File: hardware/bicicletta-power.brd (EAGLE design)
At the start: 160 x 100 mm, 24 parts, among them IC1 LM5017, IC2 LM1117-3.3

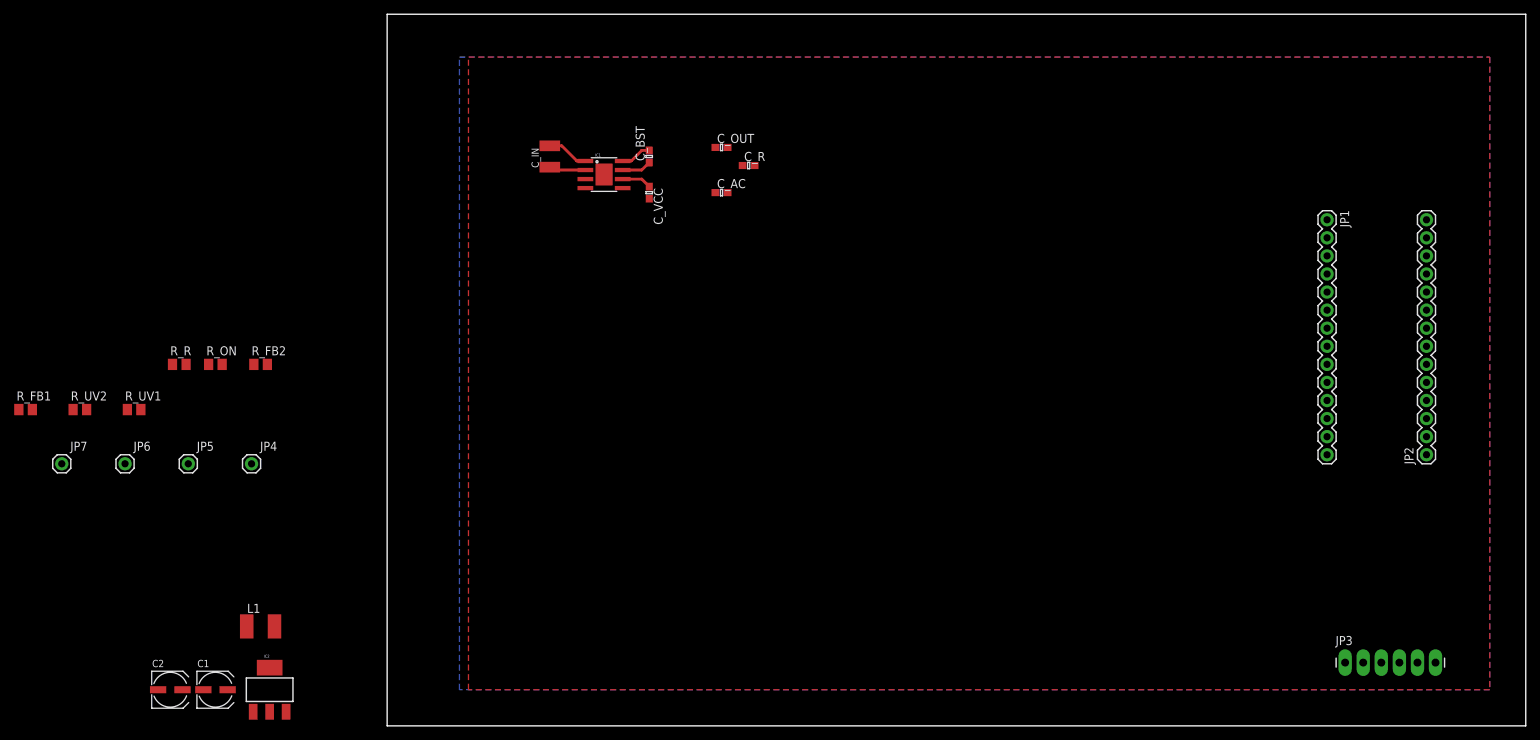
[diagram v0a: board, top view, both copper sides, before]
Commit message: Close to final layout on switching regulator.
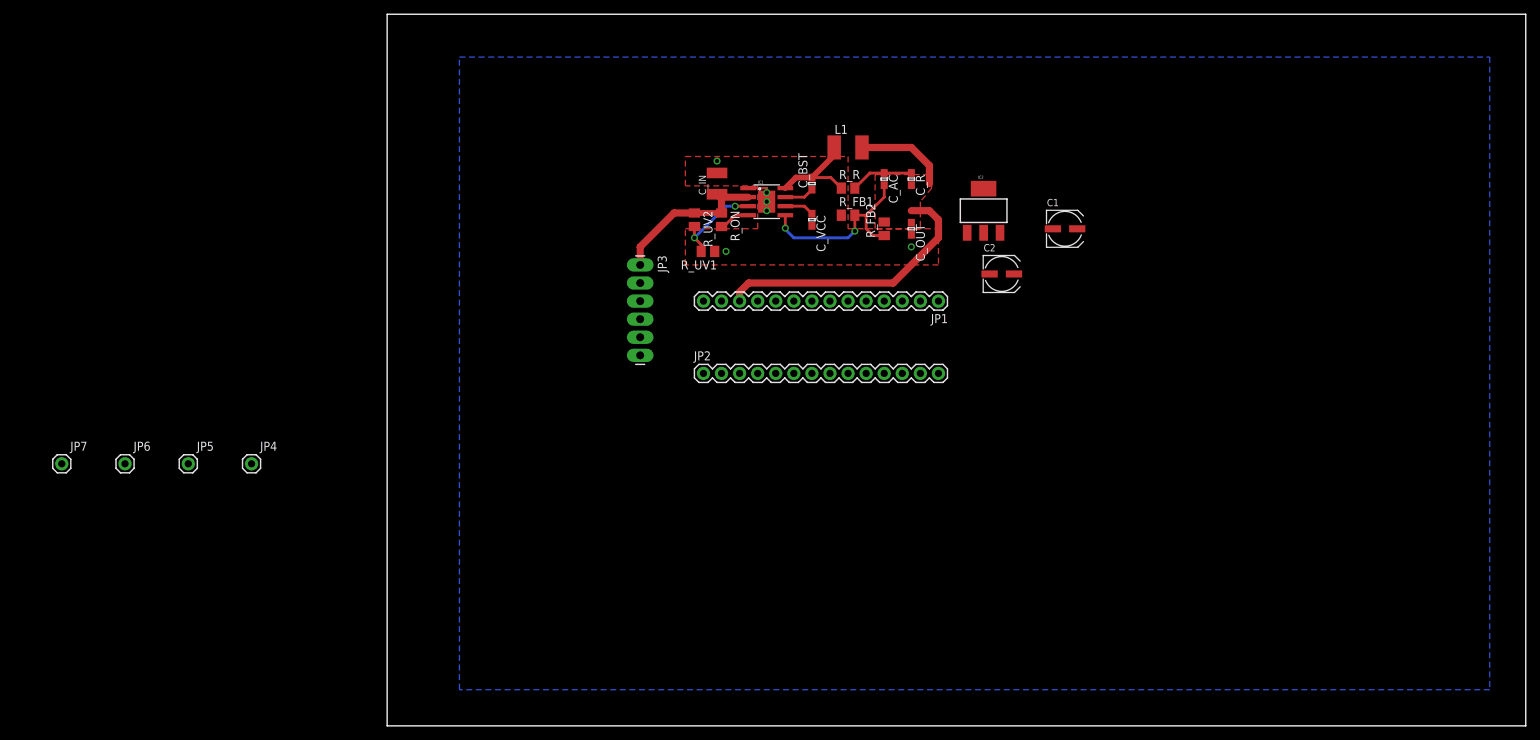
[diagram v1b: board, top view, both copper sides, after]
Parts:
- moved C1 135.8 mm to (95.2, 69.8)
- moved C2 130.6 mm to (86.4, 63.5)
- moved IC2 120.8 mm to (83.8, 72.4)
- moved R_FB1 118.8 mm to (64.8, 71.8)
- moved JP3 113.7 mm to (35.6, 64.8), turned to 270 degrees
- moved L1 106.5 mm to (64.8, 81.3)
- moved JP2 102.2 mm to (44.5, 49.5), turned to 0 degrees
- moved R_R 97.2 mm to (64.8, 75.6)
- moved R_UV2 90.4 mm to (43.2, 71.1), turned to 270 degrees
- moved R_FB2 89.7 mm to (69.8, 69.8), turned to 90 degrees
- moved R_UV1 83.7 mm to (45.1, 66.7), turned to 180 degrees
- moved R_ON 74.0 mm to (47.0, 71.1), turned to 270 degrees
- moved JP1 55.8 mm to (77.5, 59.7), turned to 180 degrees
- moved C_OUT 29.0 mm to (73.7, 69.8), turned to 270 degrees
- moved C_IN 23.8 mm to (46.4, 76.2)
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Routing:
- net 5V: track 0.00 -> 52.3 mm
- net N$2: track 0.00 -> 26.6 mm, vias 0 -> 2
- net V_BATT: track 5.17 -> 23.4 mm
- net N$3: track 0.00 -> 13.3 mm, vias 0 -> 2
- net N$4: track 4.35 -> 14.6 mm
- net N$6: track 0.00 -> 8.82 mm
- net N$1: track 0.00 -> 4.39 mm
- net GND: track 5.89 -> 3.25 mm, vias 0 -> 6
- added copper zone on layer 1, net GND

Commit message: Fine tuning
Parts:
- moved JP7 89.3 mm to (40.6, 59.7)
- moved JP6 78.3 mm to (38.1, 59.7)
- moved JP5 67.3 mm to (38.1, 49.5)
- moved JP4 61.0 mm to (40.6, 49.5)
- moved JP3 11.5 mm to (36.8, 76.2)
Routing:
- net V_BATT: track 23.4 -> 20.2 mm
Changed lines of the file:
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@@
 <element name="C_R" library="rcl" package="C0603" value="3300pF" x="73.66" y="76.835" rot="R270"/>
 <element name="C_AC" library="rcl" package="C0603" value="100nF" x="69.85" y="76.835" rot="R270"/>
-<element name="JP3" library="SparkFun-Connectors" package="1X06_LONGPADS" value="" x="35.56" y="64.77" rot="R270"/>
-<element name="JP4" library="SparkFun-Connectors" package="1X01" value="M01PTH" x="-19.05" y="36.83"/>
-<element name="JP5" library="SparkFun-Connectors" package="1X01" value="M01PTH" x="-27.94" y="36.83"/>
-<element name="JP6" library="SparkFun-Connectors" package="1X01" value="M01PTH" x="-36.83" y="36.83"/>
-<element name="JP7" library="SparkFun-Connectors" package="1X01" value="M01PTH" x="-45.72" y="36.83"/>
+<element name="JP3" library="SparkFun-Connectors" package="1X06_LONGPADS" value="" x="36.83" y="76.2" rot="R270"/>
+<element name="JP4" library="SparkFun-Connectors" package="1X01" value="M01PTH" x="40.64" y="49.53"/>
+<element name="JP5" library="SparkFun-Connectors" package="1X01" value="M01PTH" x="38.1" y="49.53"/>
+<element name="JP6" library="SparkFun-Connectors" package="1X01" value="M01PTH" x="38.1" y="59.69"/>
+<element name="JP7" library="SparkFun-Connectors" package="1X01" value="M01PTH" x="40.64" y="59.69"/>
 </elements>
 <signals>
@@
 </polygon>
 <polygon width="0.4064" layer="1" thermals="no">
-<vertex x="41.91" y="80.01"/>
+<vertex x="44.45" y="80.01"/>
 <vertex x="64.77" y="80.01"/>
 <vertex x="64.77" y="69.85"/>
@@
 <vertex x="52.07" y="69.85"/>
 <vertex x="52.07" y="75.8825"/>
-<vertex x="41.91" y="75.8825"/>
+<vertex x="44.45" y="75.8825"/>
 </polygon>
 <via x="53.34" y="73.66" extent="1-16" drill="0.6"/>
@@
 <contactref element="JP7" pad="1"/>
 <wire x1="43.18" y1="72.07" x2="46.99" y2="72.07" width="0.8128" layer="1"/>
-<wire x1="35.56" y1="64.77" x2="35.56" y2="67.31" width="1.016" layer="1"/>
-<wire x1="35.56" y1="67.31" x2="40.32" y2="72.07" width="1.016" layer="1"/>
-<wire x1="43.18" y1="72.07" x2="40.32" y2="72.07" width="1.016" layer="1"/>
+<wire x1="36.83" y1="76.2" x2="40.64" y2="76.2" width="1.016" layer="1"/>
+<wire x1="40.64" y1="76.2" x2="43.1775" y2="73.6575" width="1.016" layer="1"/>
+<wire x1="43.18" y1="72.07" x2="43.1775" y2="73.6575" width="1.016" layer="1"/>
 <wire x1="46.99" y1="72.07" x2="46.99" y2="74.065" width="1.016" layer="1"/>
 <wire x1="46.99" y1="74.065" x2="46.355" y2="74.7" width="1.016" layer="1"/>
 <wire x1="50.7238" y1="74.295" x2="46.76" y2="74.295" width="1.016" layer="1"/>
 <wire x1="46.76" y1="74.295" x2="46.355" y2="74.7" width="1.016" layer="1"/>
-<wire x1="-36.83" y1="36.83" x2="35.56" y2="64.77" width="0" layer="19" extent="1-1"/>
-<wire x1="-45.72" y1="36.83" x2="-36.83" y2="36.83" width="0" layer="19" extent="1-1"/>
+<wire x1="40.64" y1="59.69" x2="43.18" y2="72.07" width="0" layer="19" extent="1-1"/>
+<wire x1="38.1" y1="59.69" x2="40.64" y2="59.69" width="0" layer="19" extent="1-1"/>
 </signal>
 <signal name="5V">
@@
 <contactref element="JP3" pad="4"/>
 <contactref element="JP4" pad="1"/>
-<wire x1="-19.05" y1="36.83" x2="35.56" y2="57.15" width="0" layer="19" extent="1-1"/>
+<wire x1="40.64" y1="49.53" x2="36.83" y2="68.58" width="0" layer="19" extent="1-1"/>
 </signal>
 <signal name="SPEED_5">

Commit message: nudging
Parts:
- moved JP3 10.2 mm to (36.8, 66.0), turned to 90 degrees
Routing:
- net V_BATT: track 20.2 -> 31.2 mm
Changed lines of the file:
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@@
 <element name="C_R" library="rcl" package="C0603" value="3300pF" x="73.66" y="76.835" rot="R270"/>
 <element name="C_AC" library="rcl" package="C0603" value="100nF" x="69.85" y="76.835" rot="R270"/>
-<element name="JP3" library="SparkFun-Connectors" package="1X06_LONGPADS" value="" x="36.83" y="76.2" rot="R270"/>
+<element name="JP3" library="SparkFun-Connectors" package="1X06_LONGPADS" value="" x="36.83" y="66.04" rot="R90"/>
 <element name="JP4" library="SparkFun-Connectors" package="1X01" value="M01PTH" x="40.64" y="49.53"/>
 <element name="JP5" library="SparkFun-Connectors" package="1X01" value="M01PTH" x="38.1" y="49.53"/>
@@
 <vertex x="77.47" y="69.85"/>
 <vertex x="77.47" y="64.77"/>
-<vertex x="41.91" y="64.77"/>
-<vertex x="41.91" y="69.85"/>
+<vertex x="44.1325" y="64.77"/>
+<vertex x="44.1325" y="69.85"/>
 <vertex x="52.07" y="69.85"/>
 <vertex x="52.07" y="75.8825"/>
@@
 <contactref element="JP7" pad="1"/>
 <wire x1="43.18" y1="72.07" x2="46.99" y2="72.07" width="0.8128" layer="1"/>
-<wire x1="36.83" y1="76.2" x2="40.64" y2="76.2" width="1.016" layer="1"/>
-<wire x1="40.64" y1="76.2" x2="43.1775" y2="73.6575" width="1.016" layer="1"/>
-<wire x1="43.18" y1="72.07" x2="43.1775" y2="73.6575" width="1.016" layer="1"/>
 <wire x1="46.99" y1="72.07" x2="46.99" y2="74.065" width="1.016" layer="1"/>
 <wire x1="46.99" y1="74.065" x2="46.355" y2="74.7" width="1.016" layer="1"/>
 <wire x1="50.7238" y1="74.295" x2="46.76" y2="74.295" width="1.016" layer="1"/>
 <wire x1="46.76" y1="74.295" x2="46.355" y2="74.7" width="1.016" layer="1"/>
-<wire x1="40.64" y1="59.69" x2="43.18" y2="72.07" width="0" layer="19" extent="1-1"/>
-<wire x1="38.1" y1="59.69" x2="40.64" y2="59.69" width="0" layer="19" extent="1-1"/>
+<wire x1="43.18" y1="72.07" x2="41.59" y2="72.07" width="1.016" layer="1"/>
+<wire x1="41.59" y1="72.07" x2="40.64" y2="71.12" width="1.016" layer="1"/>
+<wire x1="40.64" y1="71.12" x2="40.64" y2="67.31" width="1.016" layer="1"/>
+<wire x1="40.64" y1="67.31" x2="39.37" y2="66.04" width="1.016" layer="1"/>
+<wire x1="39.37" y1="66.04" x2="36.83" y2="66.04" width="1.016" layer="1"/>
+<wire x1="40.64" y1="59.69" x2="39.37" y2="59.69" width="1.016" layer="1"/>
+<wire x1="39.37" y1="59.69" x2="38.1" y2="59.69" width="1.016" layer="1"/>
+<wire x1="39.37" y1="66.04" x2="39.37" y2="59.69" width="1.016" layer="1"/>
 </signal>
 <signal name="5V">
@@
 <contactref element="JP3" pad="4"/>
 <contactref element="JP4" pad="1"/>
-<wire x1="40.64" y1="49.53" x2="36.83" y2="68.58" width="0" layer="19" extent="1-1"/>
+<wire x1="40.64" y1="49.53" x2="36.83" y2="73.66" width="0" layer="19" extent="1-1"/>
 </signal>
 <signal name="SPEED_5">
